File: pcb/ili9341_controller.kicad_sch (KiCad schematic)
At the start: 26 parts, among them J1 USB_B_Micro, U1 ICE40UP5K-SG48ITR, U2 LM3880, U3 LD1117S33TR_SOT223, U4 LD1117S12TR_SOT223, U5 LD1117S25TR_SOT223

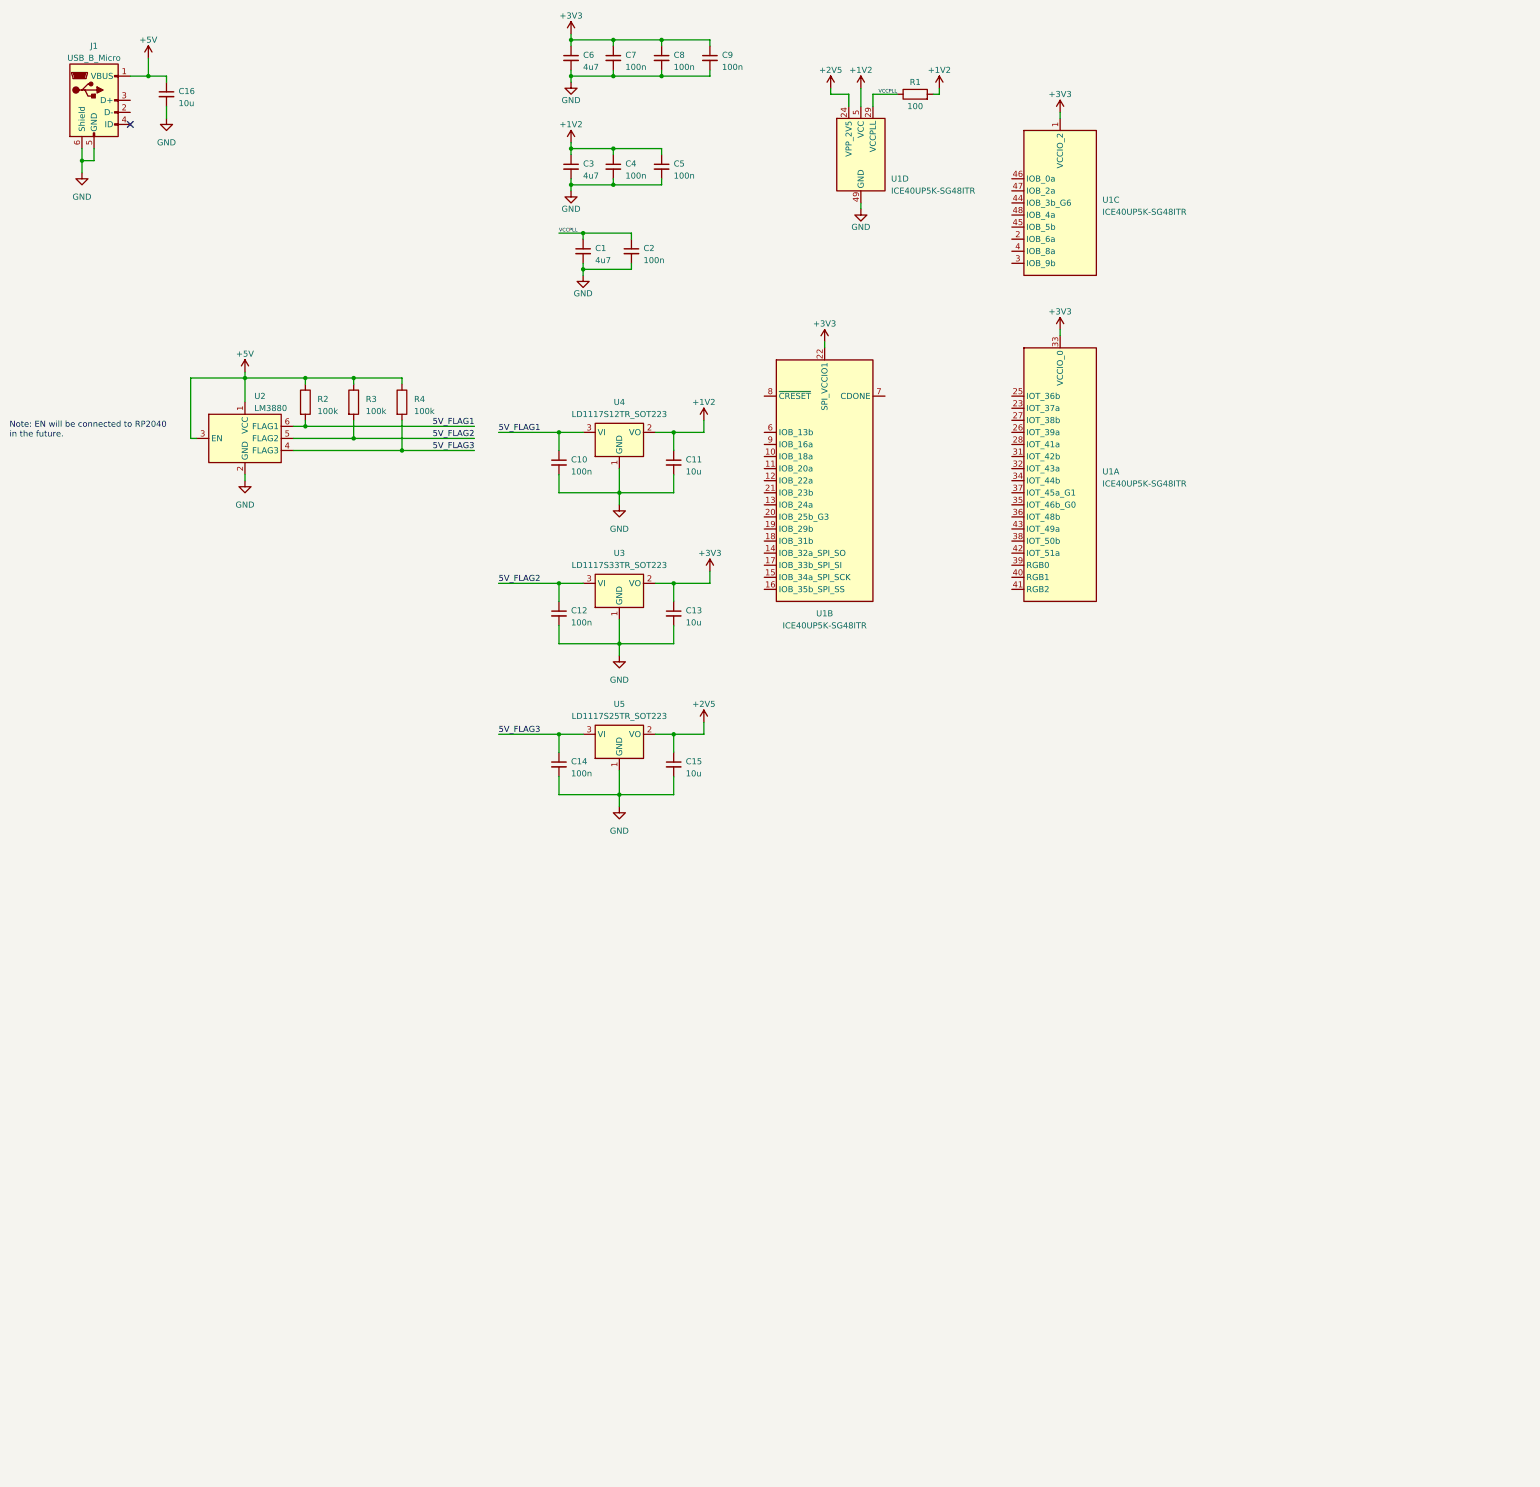
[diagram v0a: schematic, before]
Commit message: update power; add symbols for RP2040 & the TFT LCD
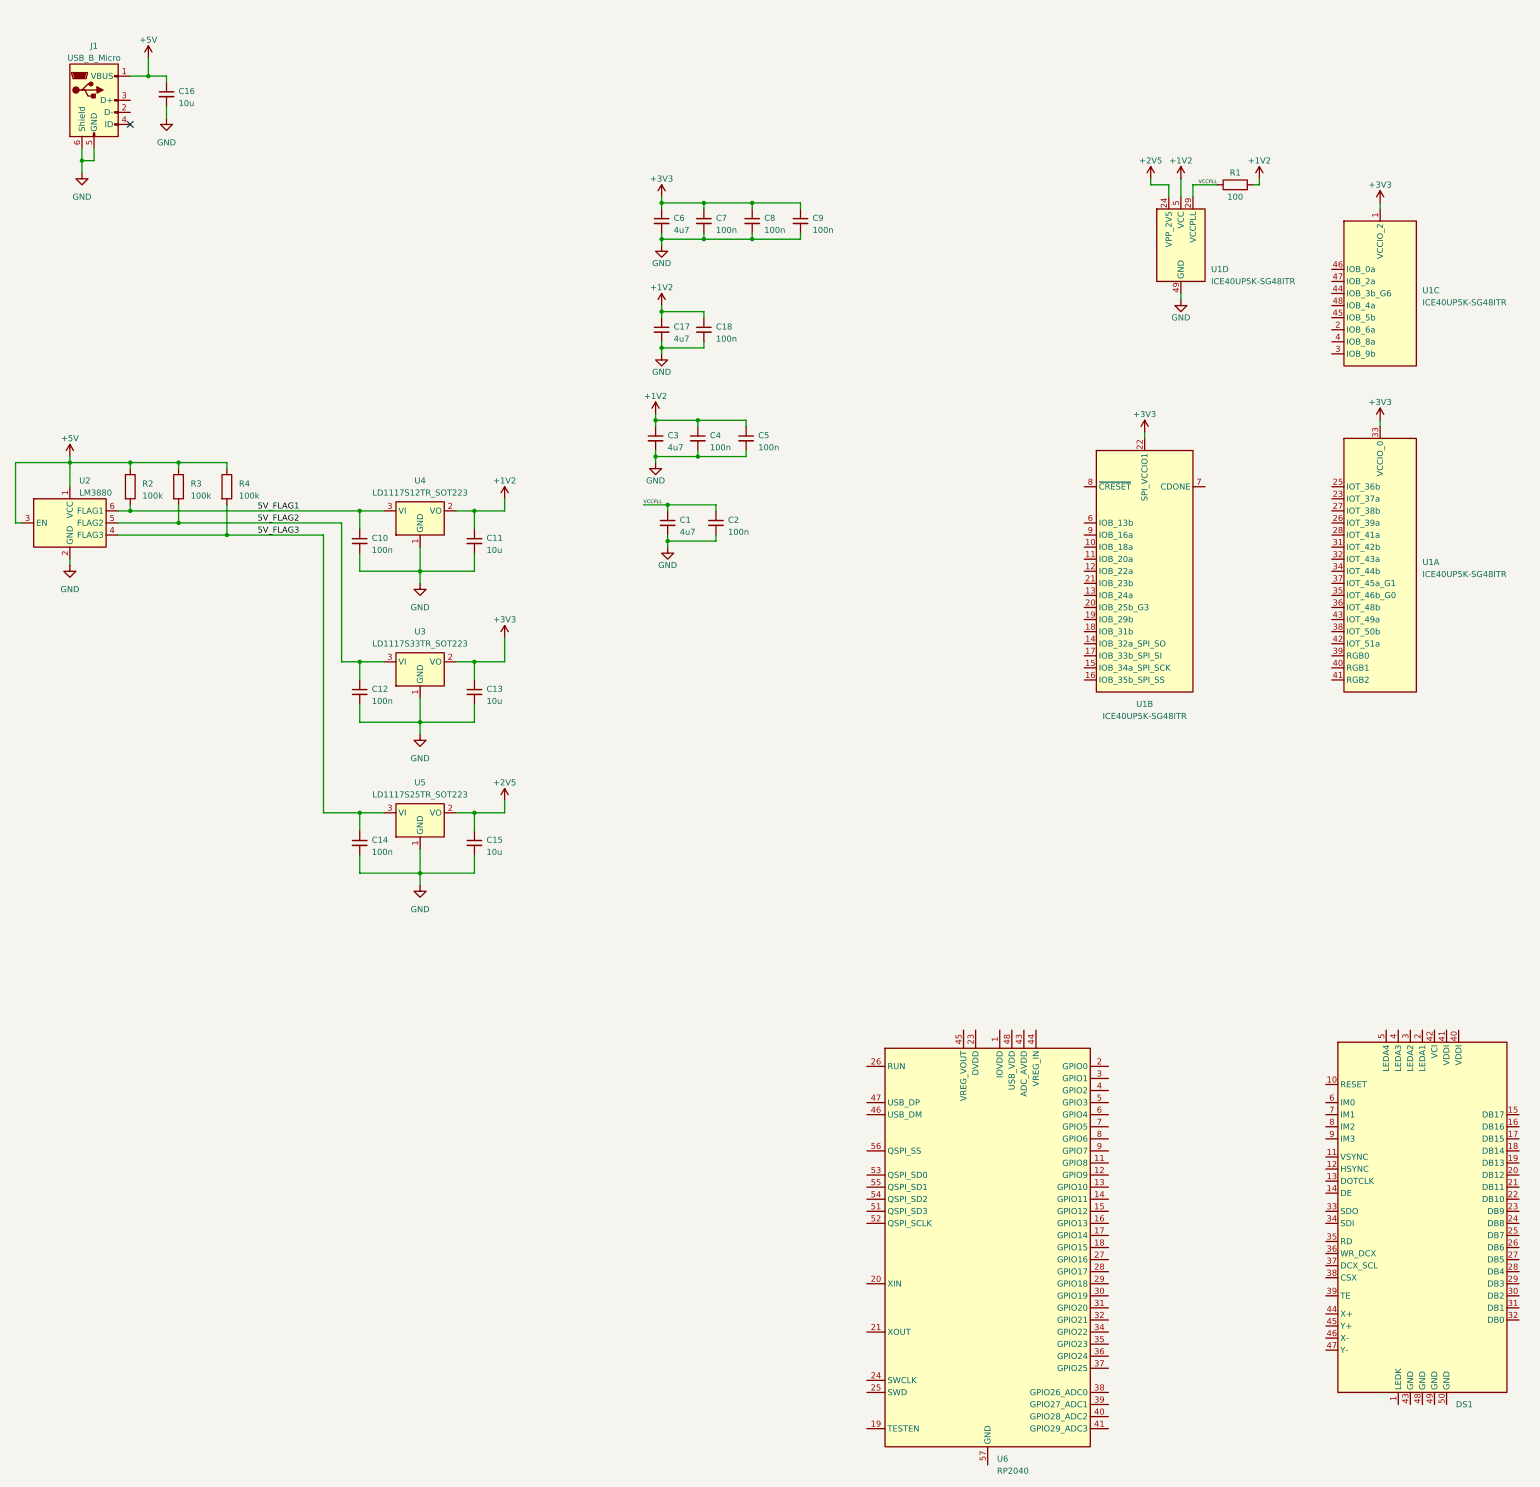
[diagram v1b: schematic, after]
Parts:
- added C17: 4u7, symbol Device:C_Small
- added C18: 100n, symbol Device:C_Small
- added DS1: ~, symbol MI0283QT-11:MI0283QT-11
- added U6: RP2040, Package_DFN_QFN:QFN-56-1EP_7x7mm_P0.4mm_EP3.2x3.2mm, symbol MCU_RaspberryPi:RP2040
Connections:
- net +1V2: now also C17.1, C18.1
- net GND: now also C17.2, C18.2
- new net: U6.1 (IOVDD), U6.10 (IOVDD), U6.22 (IOVDD), U6.33 (IOVDD), U6.42 (IOVDD), U6.49 (IOVDD)
- new net: U6.23 (DVDD), U6.50 (DVDD)
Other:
- note removed: "Note: EN will be connected to RP2040 in the future."
- moved on the sheet: C1, C10, C11, C12, C13, C14, C15, C2, C3, C4, C5, C6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

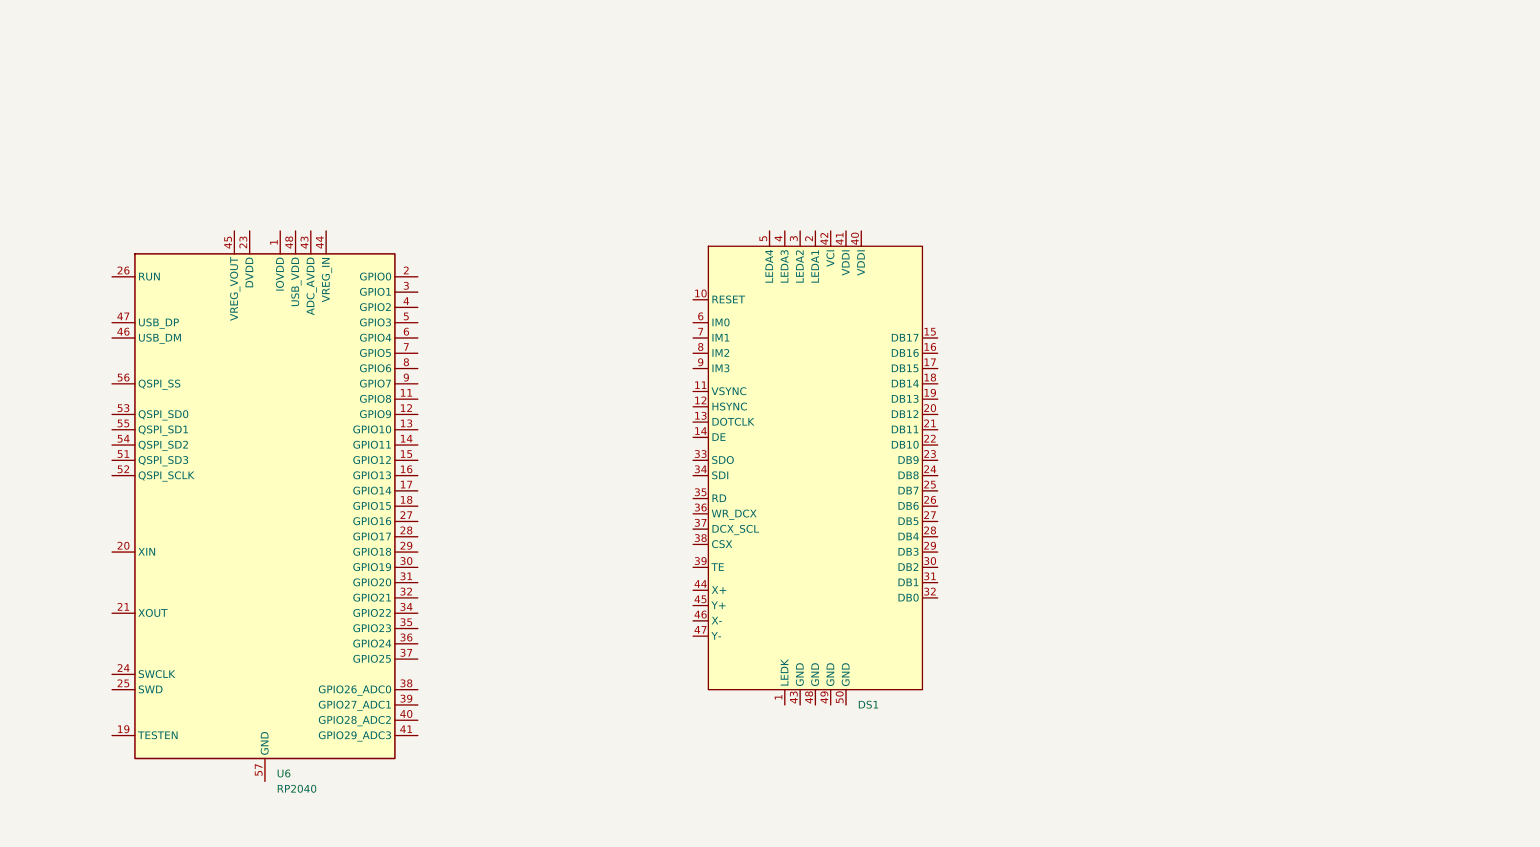
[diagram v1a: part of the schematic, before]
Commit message: add power symbols for rp2040 & tft lcd; add capacitors for rp2040
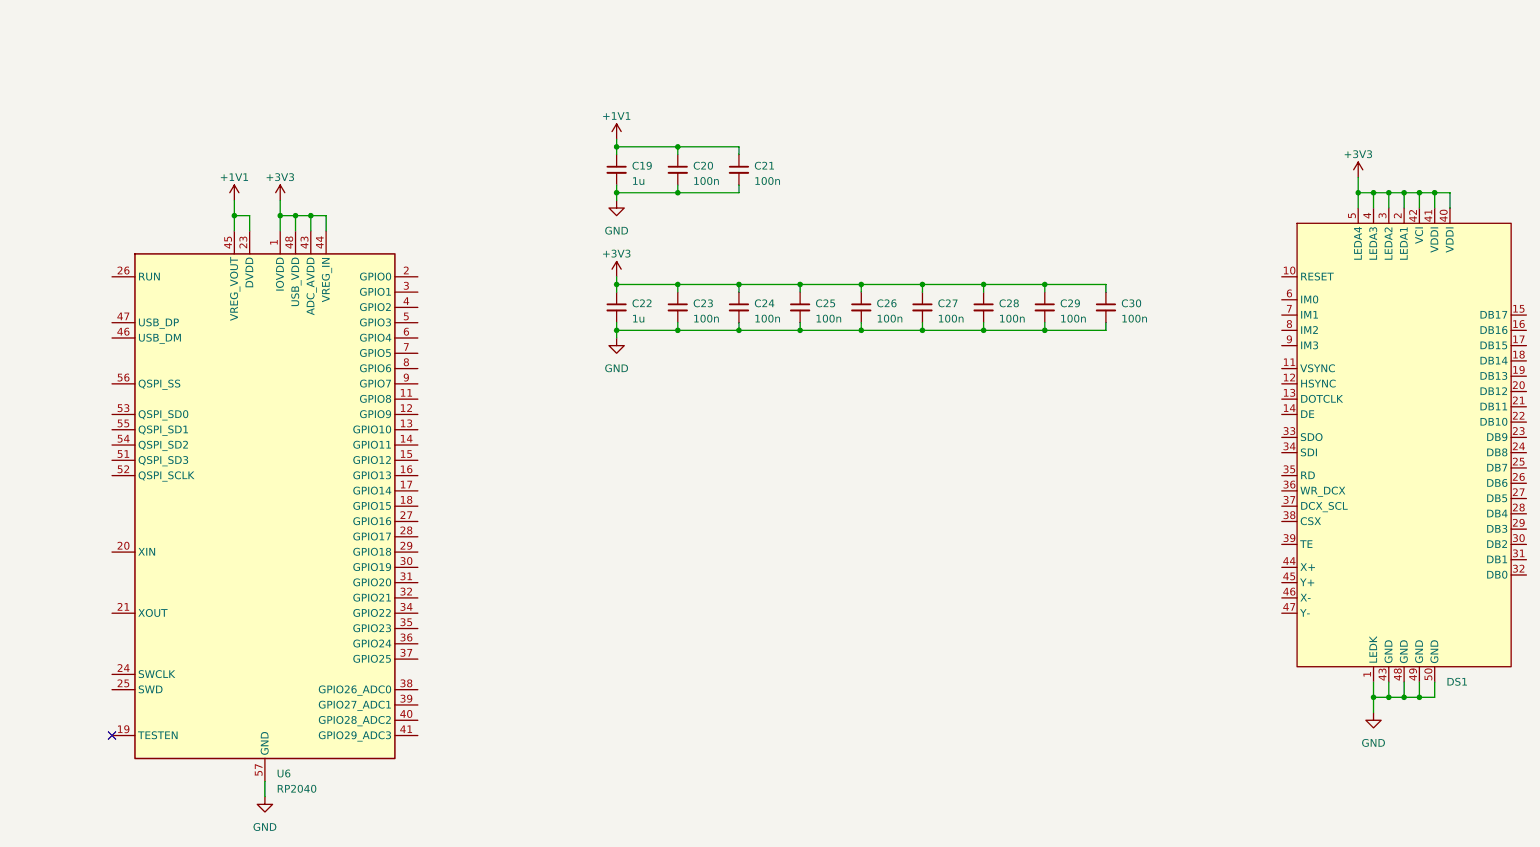
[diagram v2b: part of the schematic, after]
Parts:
- added C19, C22: 1u, symbol Device:C_Small
- added C20, C21, C23, C24, C25, C26, C27, C28, C29, C30: 100n, symbol Device:C_Small
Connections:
- net +3V3: now also DS1.2 (LEDA1), DS1.3 (LEDA2), DS1.4 (LEDA3), DS1.40 (VDDI), DS1.41 (VDDI), DS1.42 (VCI), DS1.5 (LEDA4), U6.1 (IOVDD), U6.10 (IOVDD), U6.22 (IOVDD), U6.33 (IOVDD), U6.42 (IOVDD), U6.43 (ADC_AVDD), U6.44 (VREG_IN), U6.48 (USB_VDD), U6.49 (IOVDD), C22.1, C23.1, C24.1, C25.1, C26.1, C27.1, C28.1, C29.1, C30.1
- net GND: now also DS1.1 (LEDK), DS1.43 (GND), DS1.48 (GND), DS1.49 (GND), DS1.50 (GND), U6.57 (GND), C19.2, C20.2, C21.2, C22.2, C23.2, C24.2, C25.2, C26.2, C27.2, C28.2, C29.2, C30.2
- net +1V1: now reaches U6.23 (DVDD), U6.50 (DVDD)
- net +1V1: now also U6.45 (VREG_VOUT), C19.1, C20.1, C21.1
- no-connect marks 1 -> 2
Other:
- moved on the sheet: DS1

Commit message: organize schematic
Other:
- note added: "2.5V VPP Capacitors:"
- note added: "Core VCC Capacitors:"
- note added: "FPGA Decoupling Capacitors"
- note added: "FPGA IO"
- note added: "FPGA Power"
- note added: "PLL VCC Capacitors:"
- note added: "RP2040"
- note added: "RP2040 Decoupling Capacitors"
- note added: "TFT LCD"
- note added: "USB Connector"
- note added: "VCCIO Capacitors:"
- note added: "Voltage Regulators & Power Sequencer"
- moved on the sheet: C1, C10, C11, C12, C13, C14, C15, C16, C17, C18, C19, C2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
